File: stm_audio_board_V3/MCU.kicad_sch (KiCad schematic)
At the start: 43 parts, among them J10 USB_A, SW1 SW_SPST, U1 IS42S16100H-7TL, U16 USBLC6-2P6, U17 W25Q128JVS, U19 FE1.1s, U7 STM32H723ZGTx, Y2 X1E0000210132, Y3 Crystal_GND24

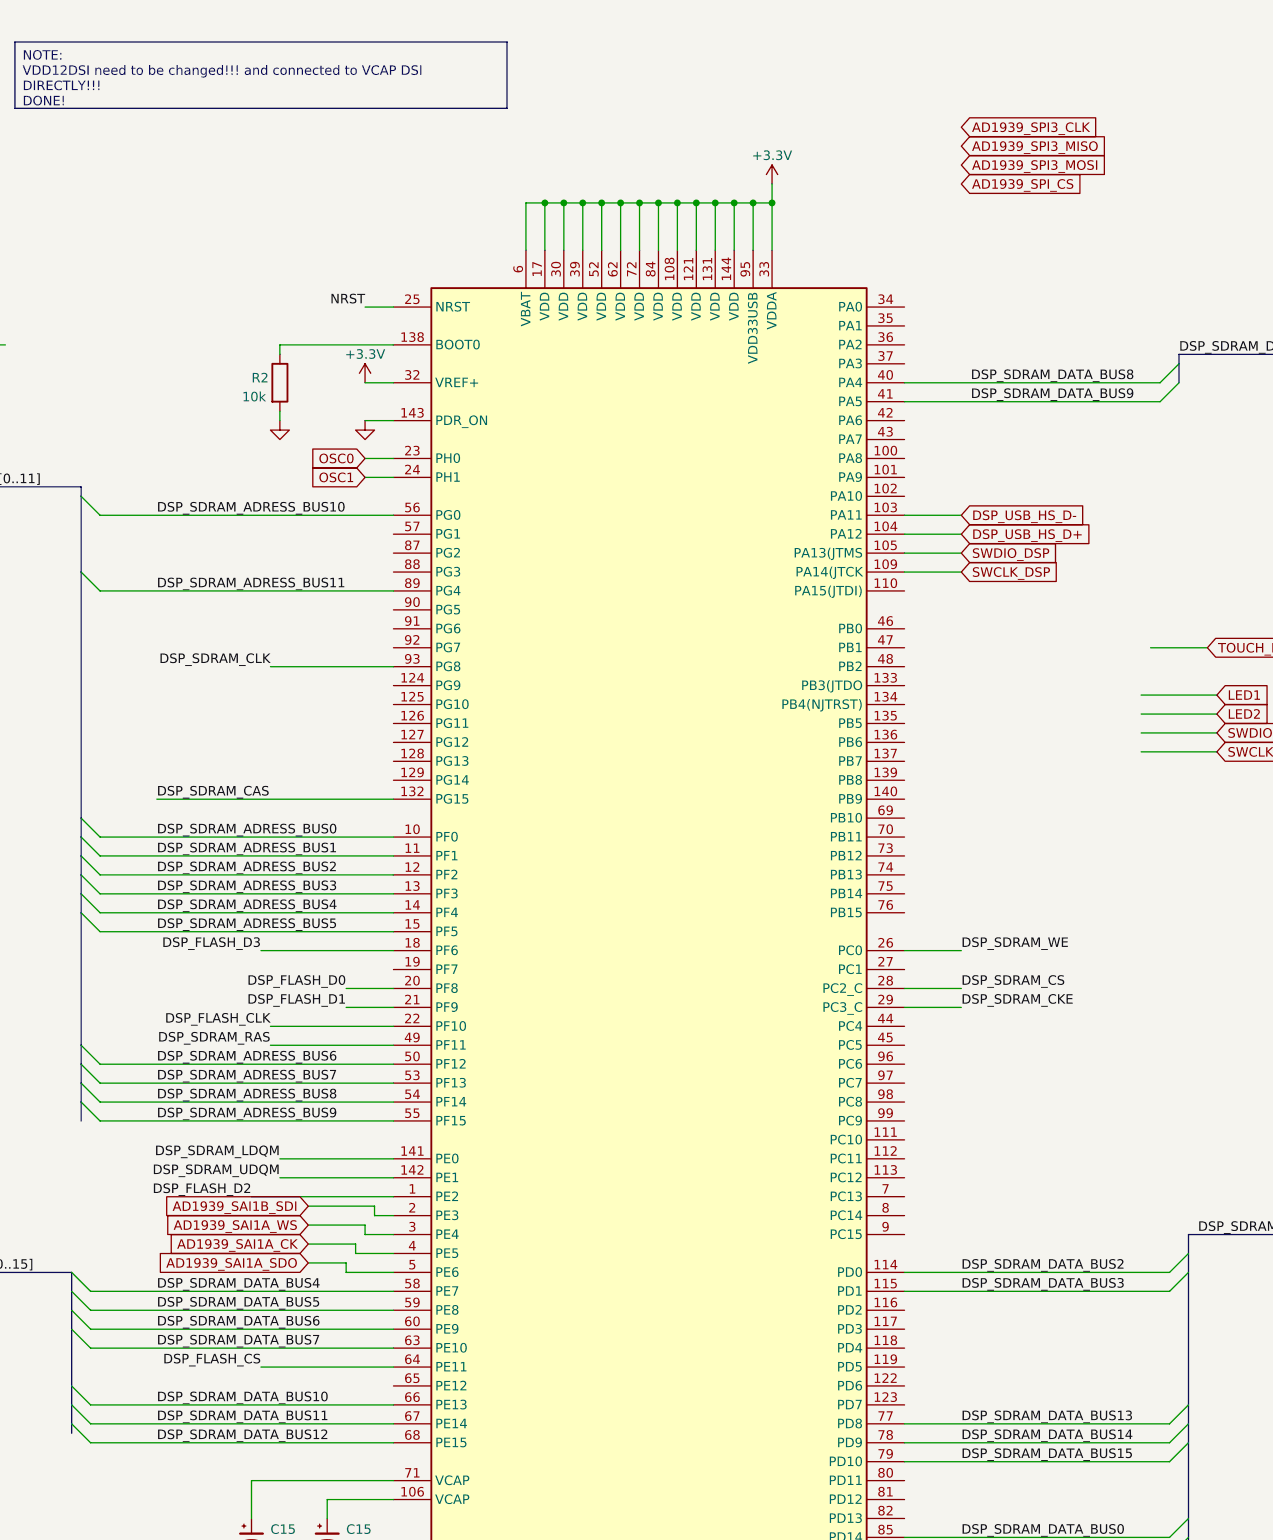
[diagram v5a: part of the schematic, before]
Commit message: Reworked outline for enclosure
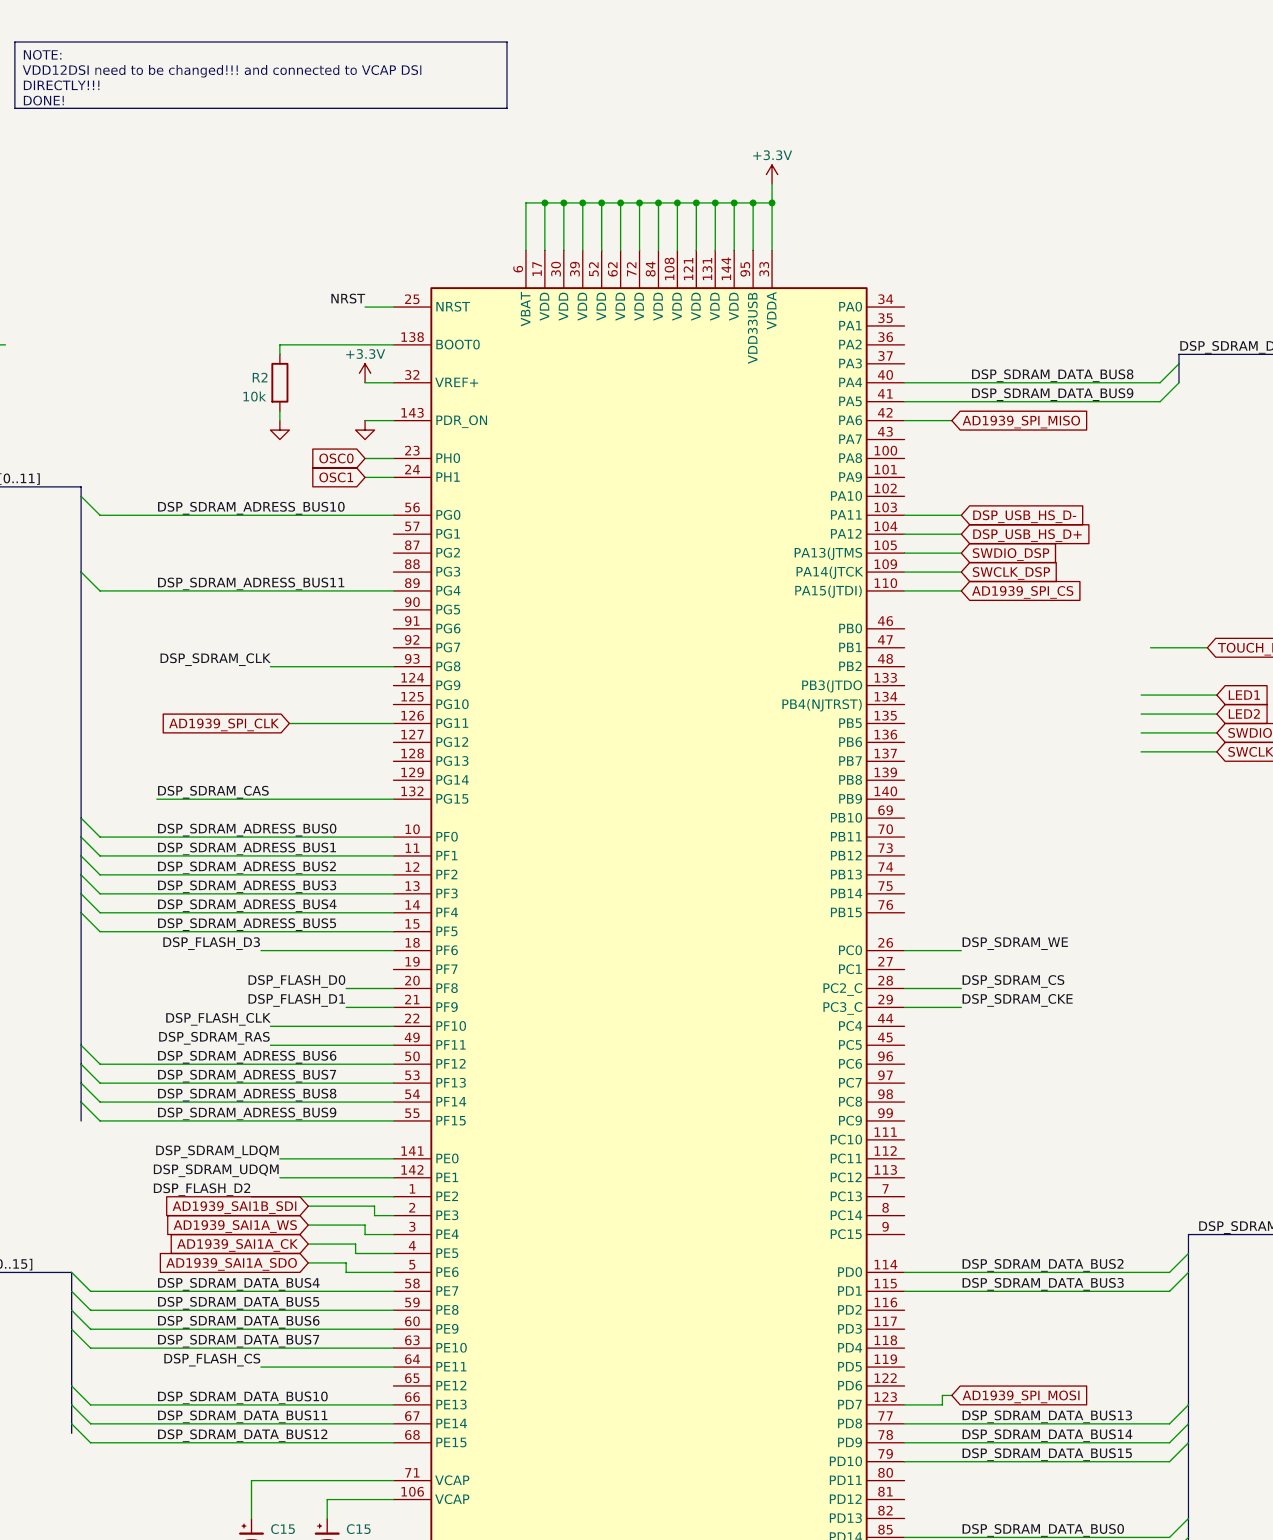
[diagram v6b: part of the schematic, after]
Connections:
- net AD1939_SPI_CS: now also U7.110 (PA15(JTDI))
- net AD1939_SPI_MOSI: now reaches U7.123 (PD7)
- net AD1939_SPI_CLK: now reaches U7.126 (PG11)
- net AD1939_SPI_MISO: now reaches U7.42 (PA6)

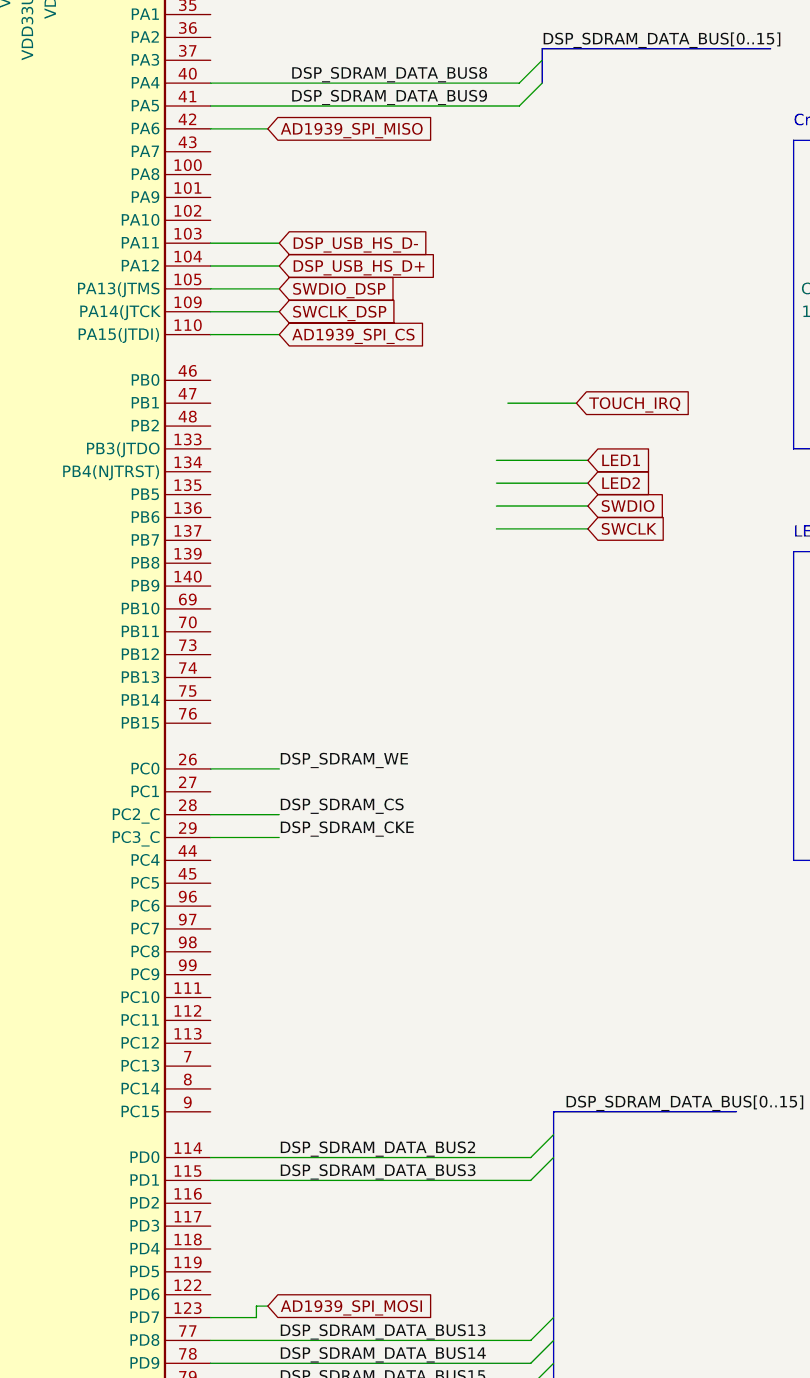
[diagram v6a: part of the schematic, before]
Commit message: gnd vias added, footswitch mux connected
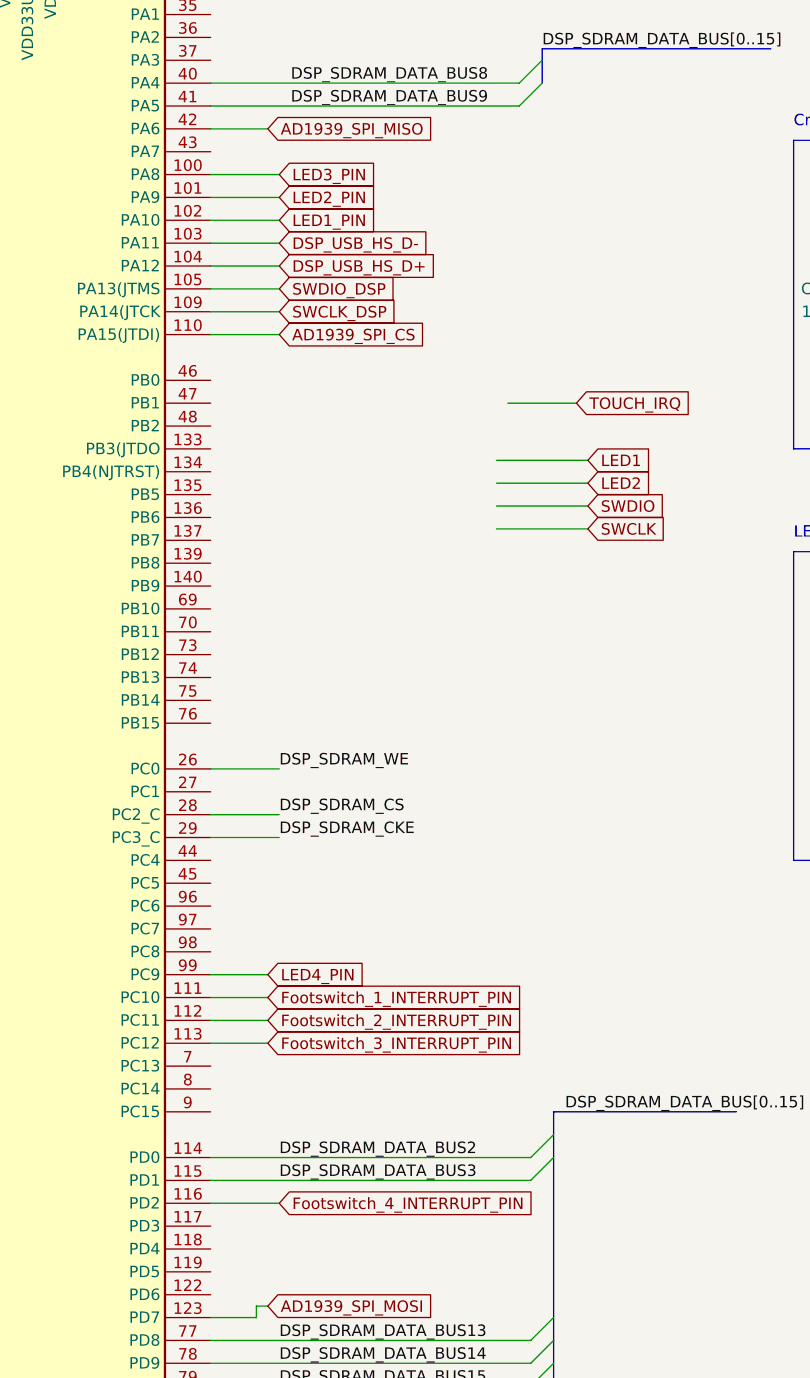
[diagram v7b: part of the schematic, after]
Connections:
- net LED3_PIN: now reaches U7.100 (PA8)
- net LED2_PIN: now reaches U7.101 (PA9)
- net LED1_PIN: now reaches U7.102 (PA10)
- net Footswitch_1_INTERRUPT_PIN: now reaches U7.111 (PC10)
- net Footswitch_2_INTERRUPT_PIN: now reaches U7.112 (PC11)
- net Footswitch_3_INTERRUPT_PIN: now reaches U7.113 (PC12)
- net Footswitch_4_INTERRUPT_PIN: now reaches U7.116 (PD2)
- net LED4_PIN: now reaches U7.99 (PC9)
